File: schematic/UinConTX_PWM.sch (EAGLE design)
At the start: 35 parts, among them J1 MICRO_USB_B_MALE_HIROSE_ZX80-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, Q4 8MHz, U1 ATMEGA328L, U2 ###V, U3 HC_05

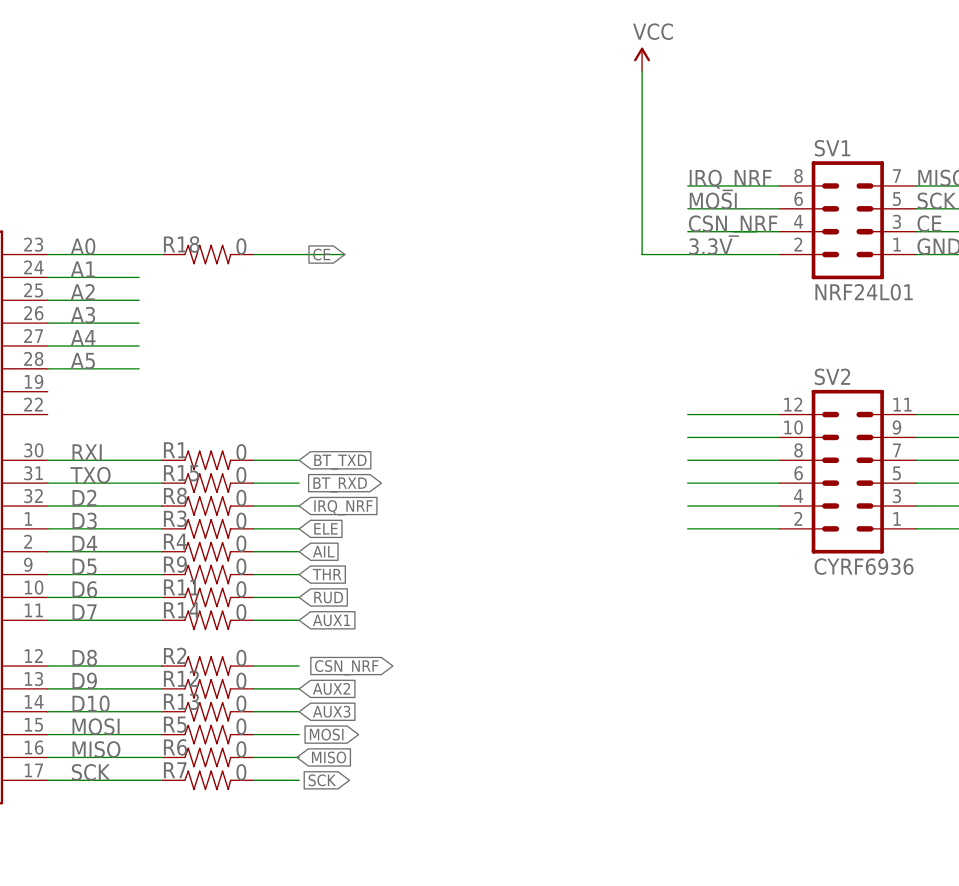
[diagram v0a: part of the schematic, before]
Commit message: ss pwm pin  changed
ss can not be used as input while spi is working
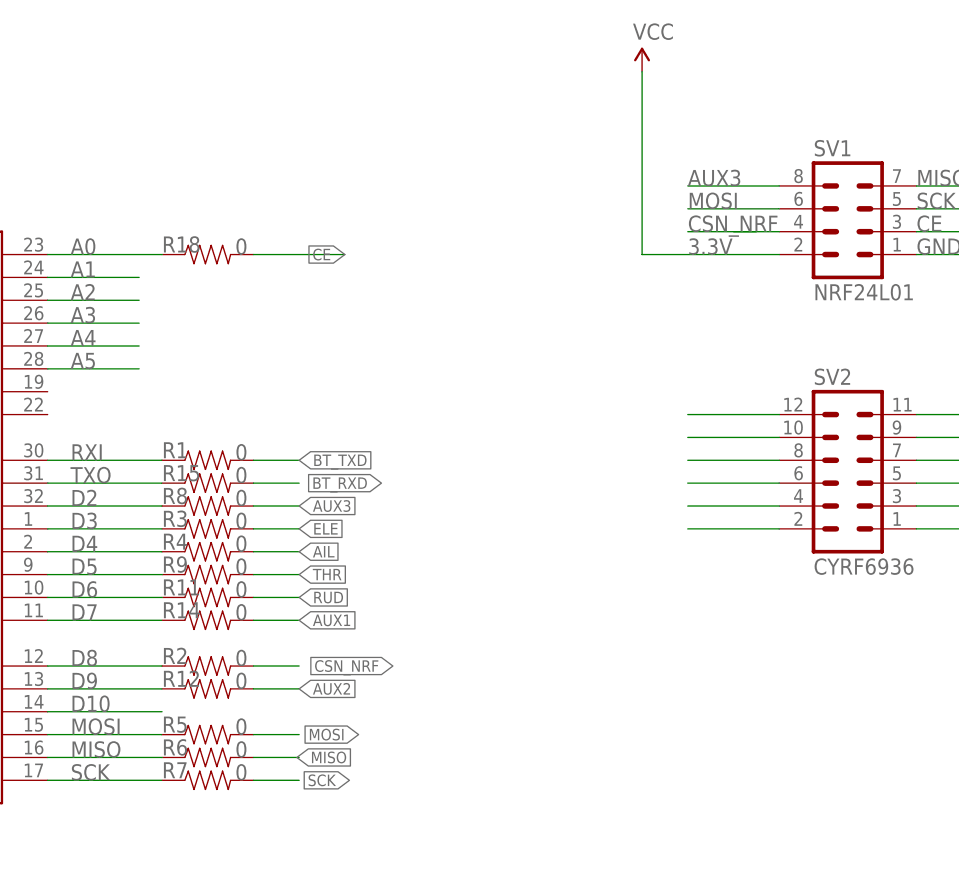
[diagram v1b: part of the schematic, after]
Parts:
- removed R13: 0, SparkFun:RESISTOR0402
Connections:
- removed net IRQ_NRF: R8.2, SV1.8
- net AUX3: now also R8.2, SV1.8; no longer R13.2
- net D10: no longer R13.1
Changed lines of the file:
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@@
 <part name="R11" library="SparkFun" deviceset="RESISTOR" device="0402" value="0"/>
 <part name="R12" library="SparkFun" deviceset="RESISTOR" device="0402" value="0"/>
-<part name="R13" library="SparkFun" deviceset="RESISTOR" device="0402" value="0"/>
 <part name="R18" library="SparkFun" deviceset="RESISTOR" device="0402" value="0"/>
 </parts>
@@
 <attribute name="VALUE" x="165.608" y="121.92" size="1.778" layer="96"/>
 </instance>
-<instance part="R13" gate="G$1" x="162.56" y="119.38" smashed="yes">
-<attribute name="NAME" x="157.48" y="119.6086" size="1.778" layer="95"/>
-<attribute name="VALUE" x="165.608" y="119.38" size="1.778" layer="96"/>
-</instance>
 <instance part="R18" gate="G$1" x="162.56" y="170.18" smashed="yes">
 <attribute name="NAME" x="157.48" y="170.4086" size="1.778" layer="95"/>
@@
 <pinref part="U1" gate="G$1" pin="PB2(SS/OC1B)"/>
 <wire x1="144.78" y1="119.38" x2="157.48" y2="119.38" width="0.1524" layer="91"/>
-<pinref part="R13" gate="G$1" pin="1"/>
 </segment>
 </net>
@@
 </segment>
 </net>
-<net name="IRQ_NRF" class="0">
+<net name="AUX3" class="0">
 <segment>
 <pinref part="SV1" gate="G$1" pin="8"/>
@@
 </segment>
 </net>
-<net name="AUX3" class="0">
-<segment>
-<pinref part="R13" gate="G$1" pin="2"/>
-<wire x1="167.64" y1="119.38" x2="172.72" y2="119.38" width="0.1524" layer="91"/>
-<label x="172.72" y="119.38" size="1.27" layer="95" xref="yes"/>
-</segment>
-</net>
